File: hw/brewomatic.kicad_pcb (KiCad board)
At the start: 2 copper layers, 95.2 x 78.7 mm, 29 parts, among them J1 CON_MAX31865, J2 EXP1, J3 EXP2, J4 12V_IN, J5 230V_CONN, J6 HEATING_CONN, J7 PUMP_CONN, J8 12V_ALIM_CONN, Q1 BT139-600, Q2 IRF540N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

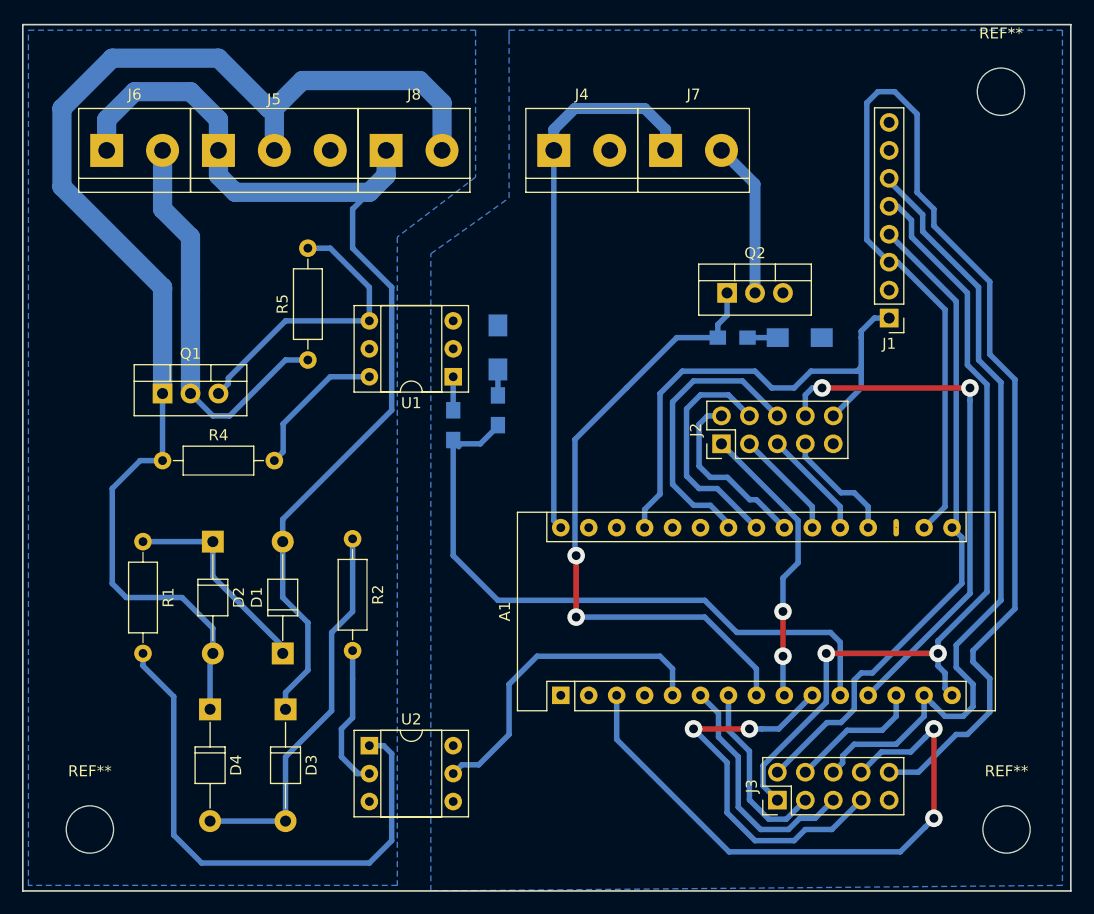
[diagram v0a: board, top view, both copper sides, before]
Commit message: Less dangerous schematic !
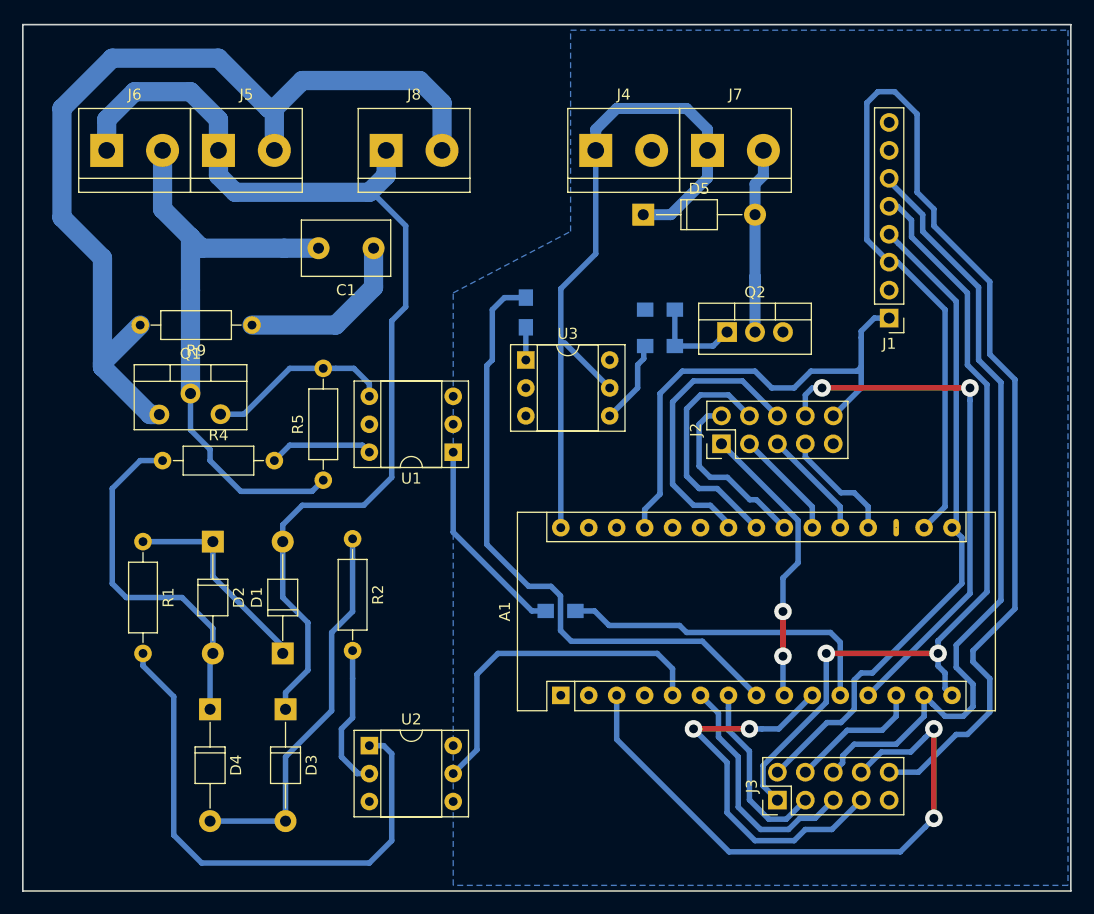
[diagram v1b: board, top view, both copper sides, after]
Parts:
- removed D6: LED_TRIAC, LEDs:LED_1206_HandSoldering
- removed REF** (x3): MountingHole_4.3mm_M4, Mounting_Holes:MountingHole_4.3mm_M4
- added C1: C, Capacitors_THT:C_Disc_D8.0mm_W5.0mm_P5.00mm, F.Cu at (148.7, 99.1)
- added R8: 10K, Resistors_SMD:R_0805_HandSoldering, B.Cu at (174.8, 104.6)
- added R9: R, Resistors_THT:R_Axial_DIN0207_L6.3mm_D2.5mm_P10.16mm_Horizontal, F.Cu at (137.7, 106.0)
- added U3: 4N25, Housings_DIP:DIP-6_W7.62mm_Socket, F.Cu at (162.6, 109.2)
- D5: value LED_PUMP -> D; footprint LEDs:LED_1206_HandSoldering -> Diodes_THT:D_T-1_P10.16mm_Horizontal; moved to F.Cu
- J5: footprint TerminalBlock:TerminalBlock_bornier-3_P5.08mm -> TerminalBlock:TerminalBlock_bornier-2_P5.08mm
- Q1: footprint TO_SOT_Packages_THT:TO-220_Vertical -> HV_TO220:TO-220_Vertical_HV
- R6: value 1K -> 470
- R7: value 1K -> 100
- moved R3 19.5 mm to (165.7, 132.0), turned to 0 degrees
- moved D5 18.1 mm to (173.2, 96.0), turned to 0 degrees
- moved R5 11.0 mm to (144.1, 120.1)
- moved R6 9.25 mm to (162.6, 104.9), turned to 90 degrees
- moved U1 6.86 mm to (156.0, 117.6)
- moved R7 6.65 mm to (174.8, 108.0)
- moved J4 3.81 mm to (168.9, 90.2)
- moved J7 3.81 mm to (179.1, 90.2)
- moved Q2 3.56 mm to (180.8, 106.7)
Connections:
- D5 pad 1: GND -> +12V
- J7 pad 2: Net-(J7-Pad2) -> Net-(D5-Pad2)
- Q2 pad 1: /PUMP_CTRL -> Net-(Q2-Pad1)
- Q2 pad 2: Net-(J7-Pad2) -> Net-(D5-Pad2)
- R6 pad 2: /TRIAC_CTRL -> /PUMP_CTRL
- R7 pad 1: Net-(D5-Pad2) -> Net-(Q2-Pad1)
- R7 pad 2: /PUMP_CTRL -> Net-(R7-Pad2)
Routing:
- net /TRIAC_CTRL: track 59.6 -> 30.1 mm
- net /HEATING_LINE: track 36.8 -> 53.9 mm
- net +12V: track 50.1 -> 67.0 mm
- net Net-(C1-Pad1): track 0.00 -> 16.0 mm
- net Net-(D5-Pad2): track 2.75 -> 18.3 mm
- net Net-(R3-Pad1): track 3.05 -> 18.6 mm
- net Net-(J7-Pad2): track 14.2 -> 0.00 mm
- net Net-(Q1-Pad3): track 26.9 -> 17.0 mm
- net Net-(Q2-Pad1): track 0.00 -> 8.70 mm
- net Net-(R7-Pad2): track 0.00 -> 7.63 mm
- net Net-(R4-Pad2): track 13.3 -> 9.48 mm
- net NEUT: track 93.9 -> 97.1 mm
- net /ZERO_CROSS_INT: track 29.9 -> 31.5 mm
- net LINE: track 117.0 -> 118.1 mm
- net /PUMP_CTRL: track 58.1 -> 57.1 mm, vias 2 -> 0
- removed copper zone on B.Cu, net Earth

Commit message: PCB: finalize layout
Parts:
- removed C1: C, Capacitors_THT:C_Disc_D8.0mm_W5.0mm_P5.00mm
- removed R9: R, Resistors_THT:R_Axial_DIN0207_L6.3mm_D2.5mm_P10.16mm_Horizontal
- added REF**: MountingHole_3mm, Mounting_Holes:MountingHole_3mm, F.Cu at (120.3, 91.1)
- added REF**: MountingHole_3mm, Mounting_Holes:MountingHole_3mm, F.Cu at (208.0, 91.3)
- added REF**: MountingHole_3mm, Mounting_Holes:MountingHole_3mm, F.Cu at (121.3, 153.0)
- added REF**: MountingHole_3mm, Mounting_Holes:MountingHole_3mm, F.Cu at (207.6, 153.0)
- R1: value R -> 45K
- R2: value R -> R45K
- moved R5 27.5 mm to (124.0, 101.5), turned to 0 degrees
- moved J8 4.30 mm to (147.4, 93.7)
- moved J5 4.23 mm to (136.9, 93.7)
- moved J6 4.03 mm to (126.4, 93.7)
- moved U2 3.69 mm to (148.2, 148.0)
- moved D1 3.69 mm to (140.3, 139.6)
- moved D2 3.69 mm to (134.0, 129.4)
- moved R1 3.69 mm to (127.6, 129.4)
- moved R2 3.69 mm to (146.7, 129.2)
- moved R4 3.69 mm to (129.4, 122.0)
- moved U1 3.69 mm to (155.8, 121.3)
- moved J1 3.56 mm to (195.5, 109.0)
- moved D5 2.92 mm to (173.4, 98.9)
- moved J4 2.92 mm to (169.0, 93.1)
- moved J7 2.92 mm to (179.2, 93.1)
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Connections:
- J6 pad 1: NEUT -> /HEATING_LINE
- J6 pad 2: /HEATING_LINE -> NEUT
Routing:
- net LINE: track 118.1 -> 80.8 mm
- net /HEATING_LINE: track 53.9 -> 19.8 mm
- net /RST: track 54.7 -> 37.7 mm, vias 2 -> 0
- net Net-(C1-Pad1): track 16.0 -> 0.00 mm
- net Net-(Q1-Pad3): track 17.0 -> 30.6 mm, vias 0 -> 2
- net +12V: track 67.0 -> 55.6 mm
- net +3V3: track 120.3 -> 112.5 mm
- net Net-(R1-Pad2): track 49.6 -> 44.9 mm
- net +5V: track 45.1 -> 41.4 mm
- net /SPI_MOSI: track 72.8 -> 69.3 mm
- net /SPI_MISO: track 77.4 -> 73.9 mm
- net /SPI_SCK: track 60.2 -> 57.0 mm
- net Net-(D5-Pad2): track 18.3 -> 15.5 mm
- net /PUMP_CTRL: track 57.1 -> 58.5 mm
- net Net-(R3-Pad1): track 18.6 -> 17.2 mm
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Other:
- board size 95.2 x 78.7 mm -> 95.2 x 70.1 mm

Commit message: PCB: fix missing TEMP_CS pin and delete sd_detect
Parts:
- moved D1 10.2 mm to (140.7, 129.4), turned to 270 degrees
- moved J6 0.25 mm to (126.6, 93.7)
- moved J8 0.25 mm to (147.2, 93.7)
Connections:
- A1 pad 10: /SD_DETECT -> /TRIAC_CTRL
- A1 pad 11: /TRIAC_CTRL -> /TEMP_CS
- J3 pad 7: /SD_DETECT -> Net-(J3-Pad7)
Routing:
- net /TEMP_CS: track 0.00 -> 66.0 mm, vias 0 -> 2
- net +3V3: track 112.5 -> 66.2 mm, vias 0 -> 2
- net /SD_DETECT: track 35.7 -> 0.00 mm, vias 2 -> 0
- net Net-(D1-Pad1): track 19.1 -> 13.1 mm
- net NEUT: track 96.0 -> 91.0 mm
- net /ZERO_CROSS_INT: track 31.5 -> 35.2 mm
- net /TRIAC_CTRL: track 30.1 -> 27.8 mm
- net /SPI_MISO: track 73.9 -> 75.0 mm
- net /RST: track 37.7 -> 38.6 mm
- net /BEEPER: vias 2 -> 0
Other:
- board text added: "BrewOMatic V0.1"

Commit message: HW: fix schematic for zero crossing input
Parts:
- removed R2: R45K, Resistors_THT:R_Axial_DIN0207_L6.3mm_D2.5mm_P10.16mm_Horizontal
- moved R3 6.06 mm to (160.1, 134.2)
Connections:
- U2 pad 2: Net-(R2-Pad2) -> Net-(D3-Pad2)
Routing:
- net +3V3: track 66.2 -> 111.5 mm, vias 2 -> 0
- net Net-(R1-Pad2): track 44.9 -> 25.9 mm
- net Net-(D3-Pad2): track 33.6 -> 15.8 mm
- net Net-(R2-Pad2): track 13.1 -> 0.00 mm
- net NEUT: track 91.0 -> 103.0 mm
- net /ZERO_CROSS_INT: track 35.2 -> 29.1 mm
- net /TRIAC_CTRL: track 27.8 -> 32.7 mm
- net /RST: track 38.6 -> 42.4 mm
- net Net-(Q1-Pad3): track 30.6 -> 27.1 mm
- net /TEMP_CS: track 66.0 -> 63.2 mm
- net Net-(R3-Pad1): track 17.2 -> 14.8 mm
- net /SPI_MOSI: track 69.3 -> 68.1 mm
- net +12V: track 55.6 -> 56.6 mm
- net /PUMP_CTRL: track 58.5 -> 59.4 mm
- net Net-(R4-Pad2): track 9.48 -> 8.95 mm

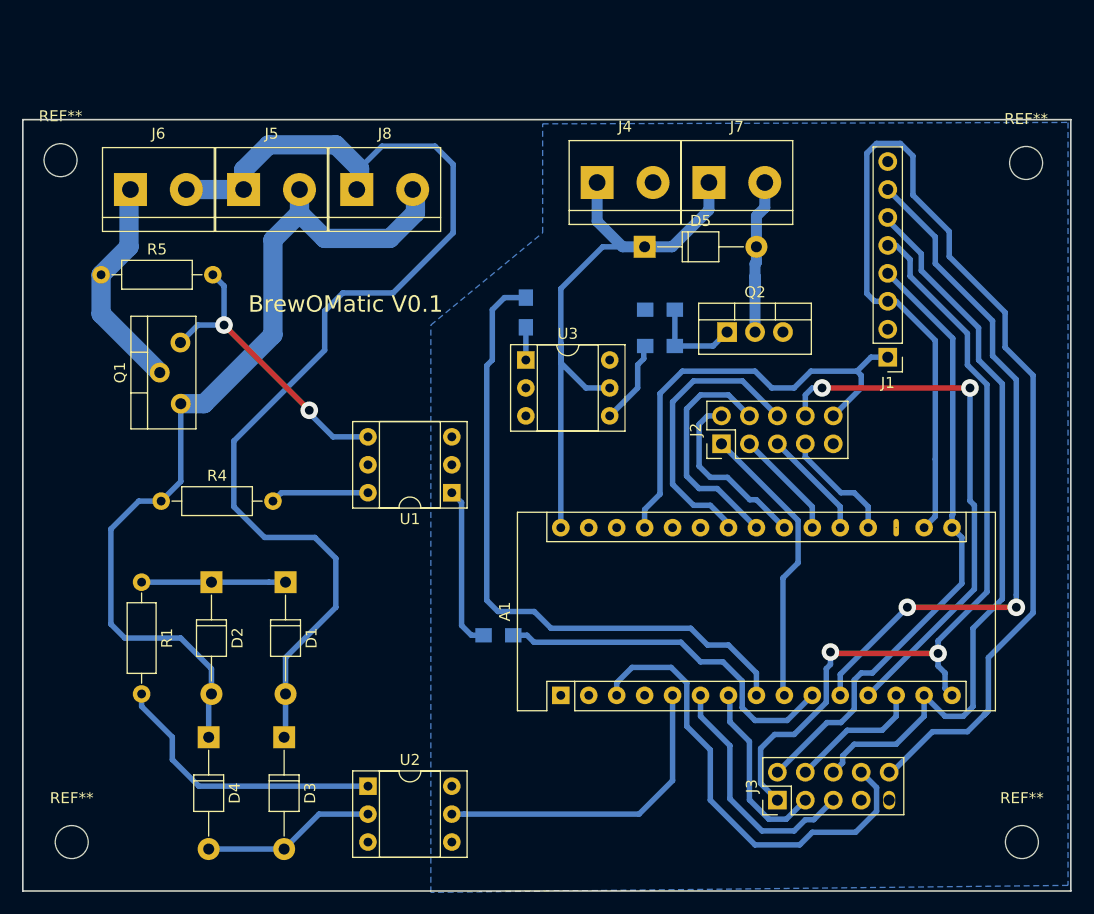
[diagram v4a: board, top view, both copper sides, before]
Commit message: PCB: update and fix LCD7/LCD5 swap
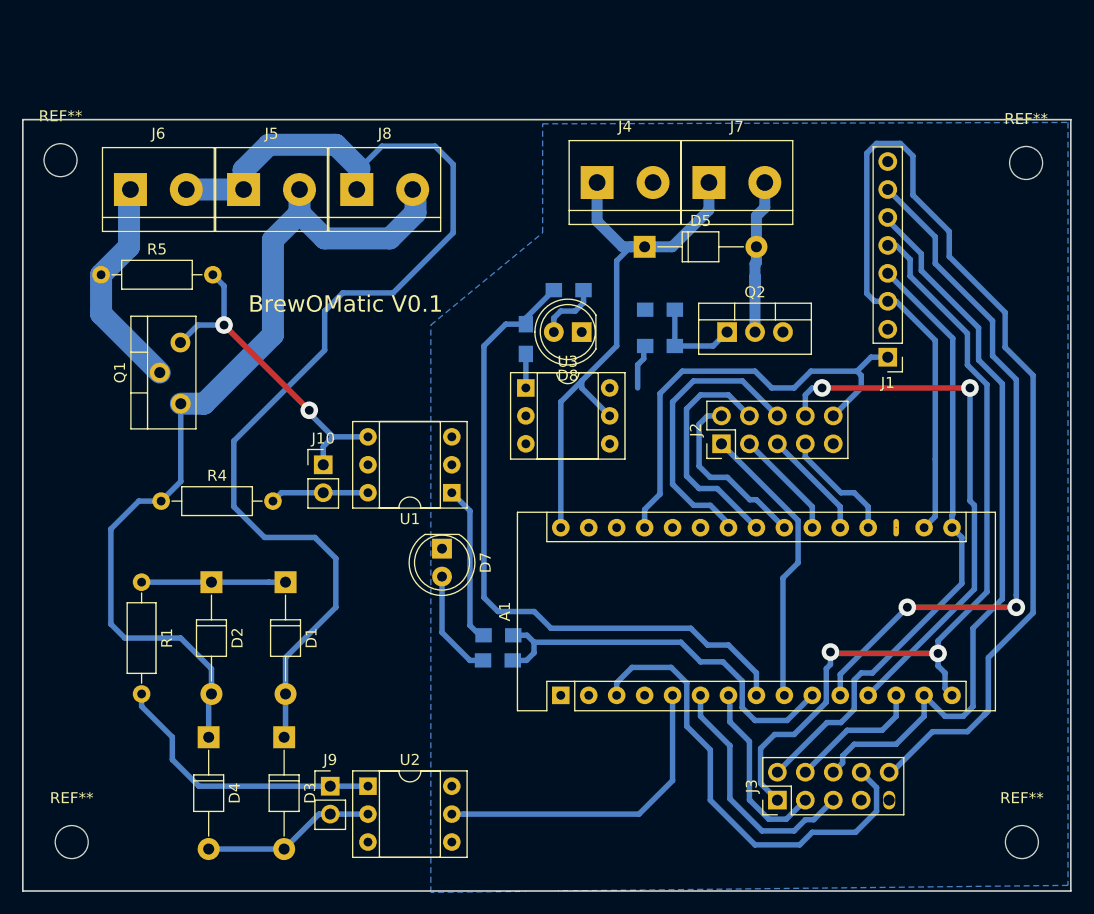
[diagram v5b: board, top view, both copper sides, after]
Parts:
- added D7: LED, LEDs:LED_D5.0mm, F.Cu at (154.9, 126.4)
- added D8: LED, LEDs:LED_D5.0mm, F.Cu at (167.6, 106.7)
- added J10: TEST_MOC, Pin_Headers:Pin_Header_Straight_1x02_Pitch2.54mm, F.Cu at (144.1, 118.7)
- added J9: TEST_IN, Pin_Headers:Pin_Header_Straight_1x02_Pitch2.54mm, F.Cu at (144.8, 148.0)
- added R10: 220, Resistors_SMD:R_0805_HandSoldering, B.Cu at (166.4, 102.9)
- added R9: 220, Resistors_SMD:R_0805_HandSoldering, B.Cu at (160.0, 136.5)
- moved U3 2.54 mm to (162.6, 111.8)
- moved R6 2.41 mm to (162.6, 107.3)
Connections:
- A1 pad 12: /LCD5 -> /LCD7
- A1 pad 24: /LCD7 -> /LCD5
- J2 pad 6: /LCD7 -> /LCD5
- J2 pad 8: /LCD5 -> /LCD7
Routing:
- net /LCD7: track 26.1 -> 49.2 mm, vias 0 -> 2
- net /LCD5: track 49.2 -> 26.1 mm, vias 2 -> 0
- net Net-(D7-Pad2): track 0.00 -> 9.86 mm
- net +12V: track 56.6 -> 50.9 mm
- net Net-(D8-Pad2): track 0.00 -> 5.70 mm
- net Net-(R7-Pad2): track 7.63 -> 4.04 mm
- net /TRIAC_CTRL: track 32.7 -> 35.9 mm
- net /PUMP_CTRL: track 59.4 -> 61.3 mm
- net Net-(J10-Pad1): track 0.00 -> 1.65 mm
- net Net-(Q1-Pad3): track 27.1 -> 28.3 mm

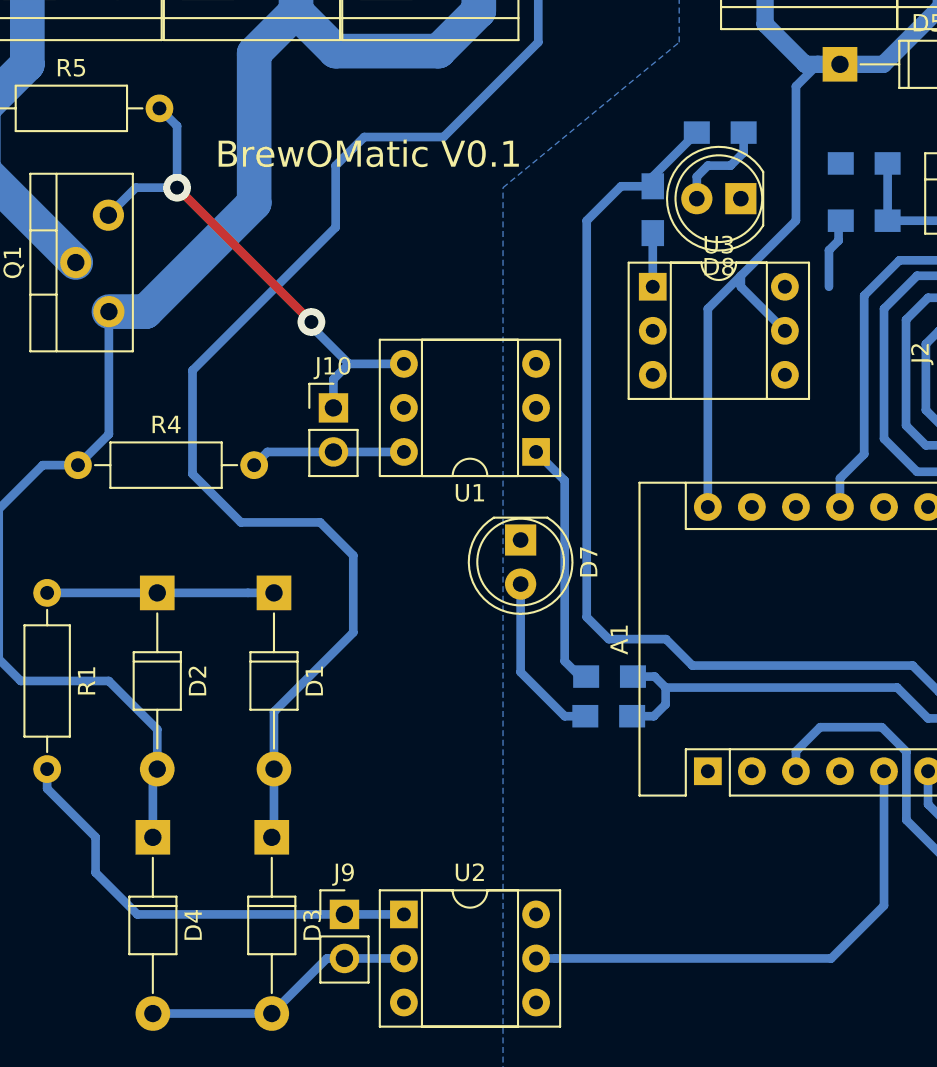
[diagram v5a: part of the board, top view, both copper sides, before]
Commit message: Fix wrong pcb connection pcb
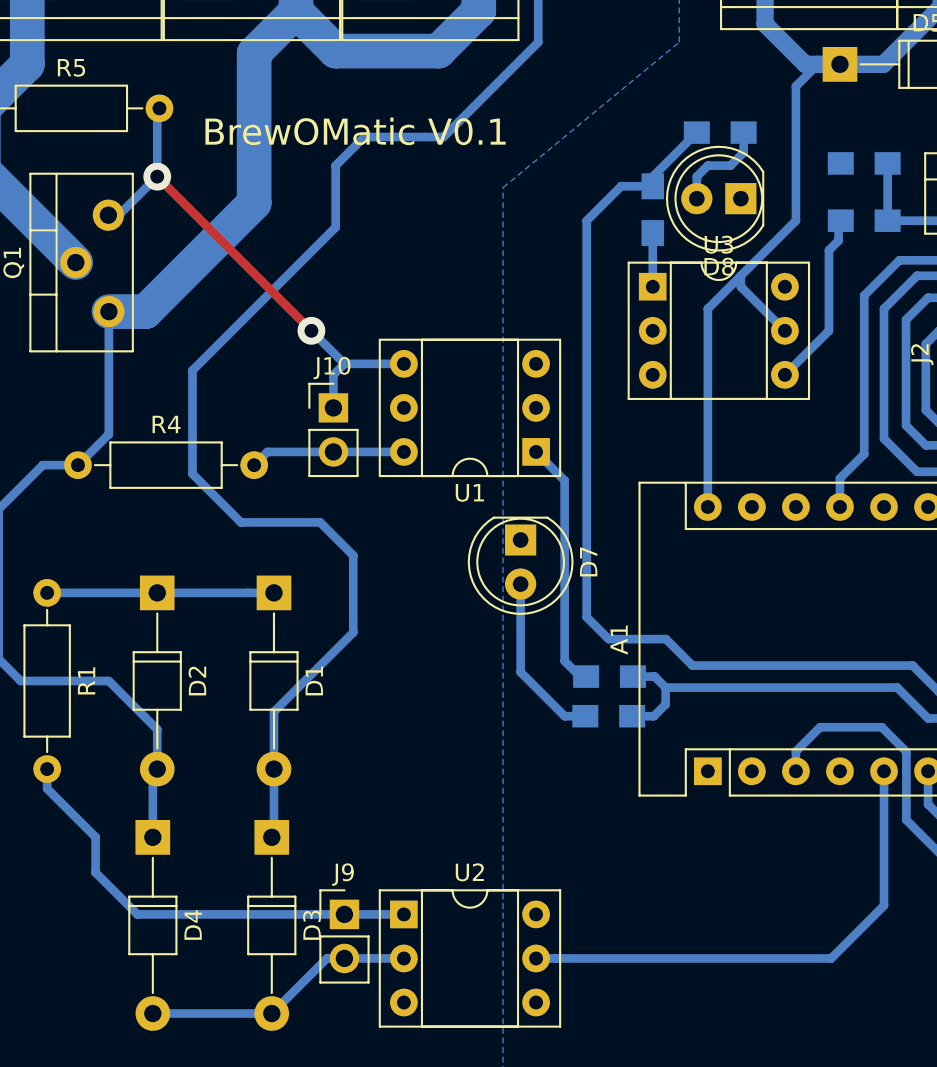
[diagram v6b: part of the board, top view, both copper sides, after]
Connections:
- A1 pad 1: Net-(A1-Pad1) -> (no net)
- A1 pad 18: Net-(A1-Pad18) -> (no net)
- A1 pad 2: Net-(A1-Pad2) -> (no net)
- A1 pad 25: Net-(A1-Pad25) -> (no net)
- A1 pad 26: Net-(A1-Pad26) -> (no net)
- A1 pad 28: Net-(A1-Pad28) -> (no net)
- J1 pad 8: /TEMP_DRDY -> (no net)
- J3 pad 7: Net-(J3-Pad7) -> (no net)
- J9 pad 2: Net-(J9-Pad2) -> Net-(D3-Pad2)
- Q1 pad 3: Net-(Q1-Pad3) -> Net-(J10-Pad1)
- R1 pad 2: Net-(R1-Pad2) -> Net-(J9-Pad1)
- R4 pad 2: Net-(R4-Pad2) -> Net-(J10-Pad2)
- R5 pad 2: Net-(Q1-Pad3) -> Net-(J10-Pad1)
- U1 pad 3: Net-(U1-Pad3) -> (no net)
- U1 pad 4: Net-(Q1-Pad3) -> Net-(J10-Pad1)
- U1 pad 5: Net-(U1-Pad5) -> (no net)
- U1 pad 6: Net-(R4-Pad2) -> Net-(J10-Pad2)
- U2 pad 1: Net-(R1-Pad2) -> Net-(J9-Pad1)
- U2 pad 3: Net-(U2-Pad3) -> (no net)
- U2 pad 6: Net-(U2-Pad6) -> (no net)
- U3 pad 3: Net-(U3-Pad3) -> (no net)
- U3 pad 6: Net-(U3-Pad6) -> (no net)
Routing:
- net Net-(Q1-Pad3): track 28.3 -> 0.00 mm, vias 2 -> 0
- net Net-(J10-Pad1): track 1.65 -> 29.2 mm, vias 0 -> 2
- net Net-(R1-Pad2): track 25.9 -> 0.00 mm
- net Net-(J9-Pad1): track 0.00 -> 25.9 mm
- net Net-(R4-Pad2): track 8.95 -> 0.00 mm
- net Net-(J10-Pad2): track 0.00 -> 8.95 mm
- net Net-(R7-Pad2): track 4.04 -> 10.2 mm
